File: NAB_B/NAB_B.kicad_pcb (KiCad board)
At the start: 2 copper layers, 35 x 30 mm, 44 parts, among them K1 кнопка, K2 кнопка, X1 Check_point

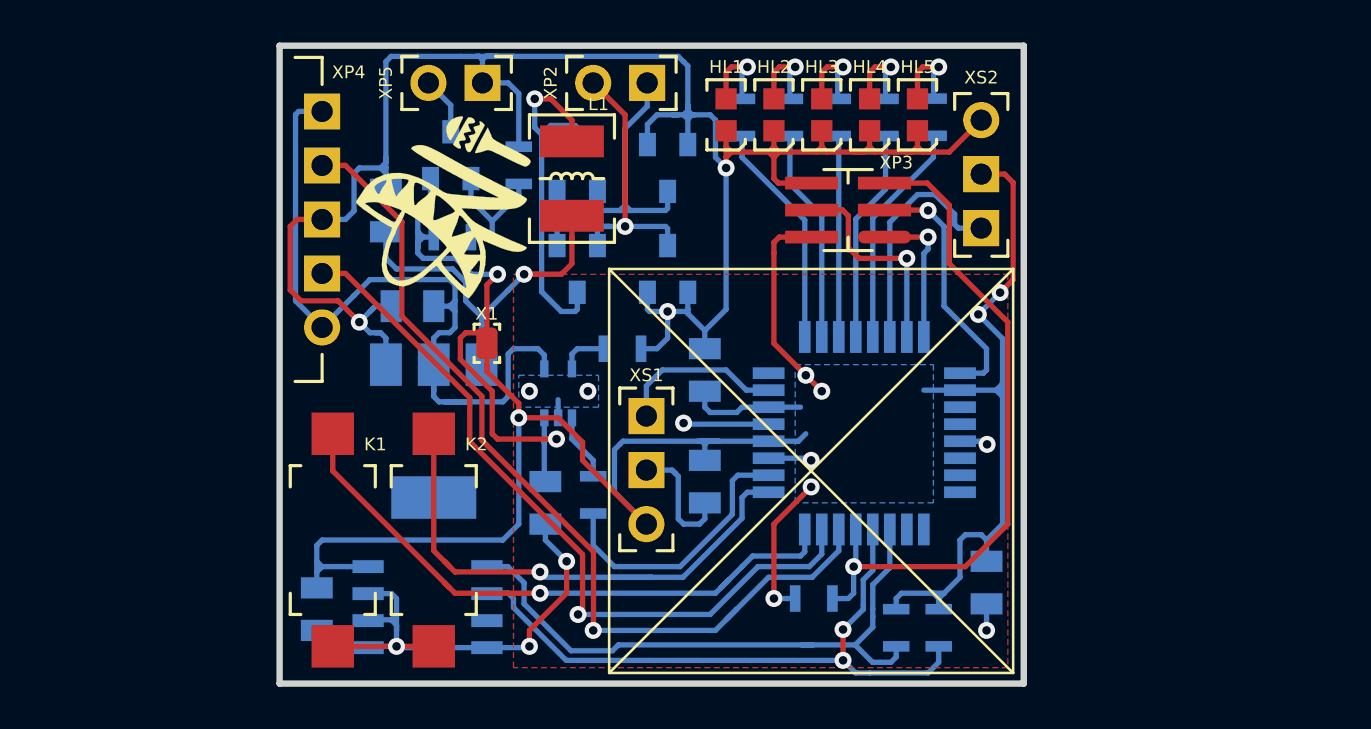
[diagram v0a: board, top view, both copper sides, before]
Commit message: NAB_A: добавить оцифровку заряда, NAB_B: прототип взят от _A
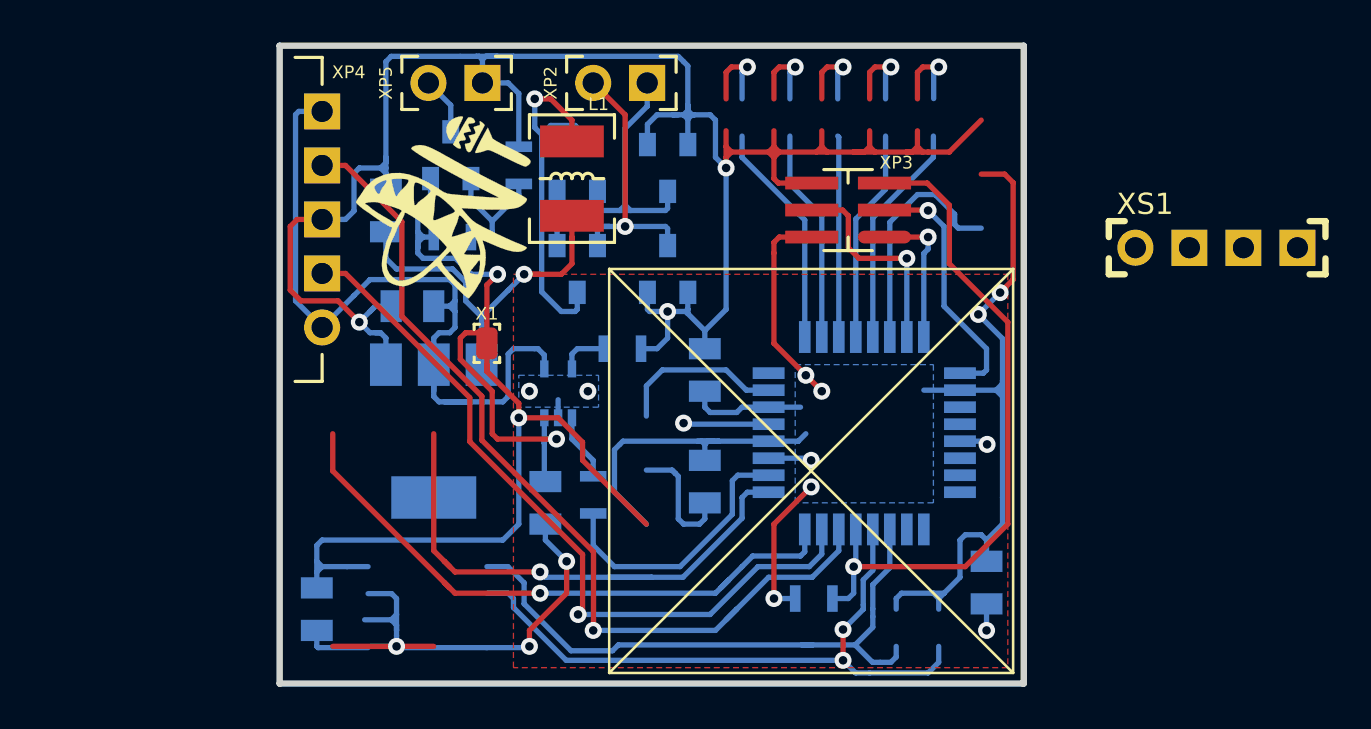
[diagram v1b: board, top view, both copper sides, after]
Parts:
- removed BK1: Преобразователь_температуры_LM75AD, N_DD:SO-8
- removed HL1, HL2, HL3, HL4, HL5: Светодиод, N_VD_HL:Светодиод_SMD_0603
- removed K1, K2: кнопка, N_X:Кнопка_FSMSM
- removed R1, R11, R12, R2, R3, R4, R5: Резистор_0,065Вт, N_RLC:Резистор_SMD_0603_0,065_Вт
- removed XS2: Розетка_PBS3, N_X:Розетка_PBS3_вертикальная
- XS1: value Розетка_PBS3 -> Розетка_PBS4; footprint N_X:Розетка_PBS3_вертикальная -> N_X:Вилка_PLS4_вертикальная
- moved XS1 26.4 mm to (250.2, 49.5), turned to 0 degrees
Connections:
- XS1 pad 1: /MC_VCC -> Net-(XS1-Pad1)
- XS1 pad 2: /GND -> Net-(XS1-Pad2)
- XS1 pad 3: /TX_DATA -> Net-(XS1-Pad3)

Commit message: NAB_B: сформированы требования к плате
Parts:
- removed the XP4 at (212.0, 43.1)
- added K1: кнопка, N_X:Кнопка_FSMSM, F.Cu at (212.5, 58.2)
- added K2: кнопка, N_X:Кнопка_FSMSM, F.Cu at (217.2, 58.2)
- added R3: Резистор_0,065Вт, N_RLC:Резистор_SMD_0603_0,065_Вт, B.Cu at (232.5, 67.5)
- added R4: Резистор_0,065Вт, N_RLC:Резистор_SMD_0603_0,065_Вт, B.Cu at (234.8, 65.8)
- added X2: Check_point, N_X:Пробник, F.Cu at (221.8, 54.0)
- added XP1: Вилка_PLS6, N_X:Вилка_PLS6_вертикальная, F.Cu at (212.0, 42.5)
- moved XS1 50.0 mm to (200.2, 51.5)
- moved R5 7.11 mm to (229.0, 67.2)
- moved C5 1.75 mm to (243.2, 62.5)
- moved L1 1.03 mm to (224.0, 45.5)
- moved DD1 1.00 mm to (233.2, 60.0)
- moved XP4 1.00 mm to (236.5, 49.0)
- moved LOGO1 0.50 mm to (218.2, 47.5)
- renumbered C3 to C1, C1 to C2, C5 to C3, C2 to C4, C6 to C5, C4 to C6, DD2 to G2, R13 to R1, R14 to R2, R9 to R5, R10 to R7, VT2 to VT1, XP5 to XP3, XP3 to XP4
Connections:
- net /TX_DATA renamed Net-(DD1-Pad7)
- DD1 pad 1: /BUT-2 -> /BUTT-2
- DD1 pad 26: Net-(DD1-Pad26) -> /VBAT_MEASUR
- DD1 pad 32: /BUT-1 -> /BUTT-1
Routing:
- net /BUT-1: track 29.6 -> 0.00 mm, vias 1 -> 0
- net /BUTT-1: track 0.00 -> 28.9 mm, vias 0 -> 1
- net /BUT-2: track 26.3 -> 0.00 mm, vias 1 -> 0
- net /BUTT-2: track 0.00 -> 25.8 mm, vias 0 -> 1
- net /MC_VCC: track 103.9 -> 123.8 mm
- net /MC_TX: track 35.6 -> 51.9 mm
- net /VBAT_MEASUR: track 0.00 -> 13.2 mm, vias 0 -> 2
- net Net-(DD1-Pad7): track 7.87 -> 0.00 mm
- net /nRESET: track 32.8 -> 40.3 mm
- net /GND: track 147.6 -> 151.9 mm, vias 12 -> 14
- net /SCL: track 30.7 -> 34.6 mm
- net /5V: track 37.3 -> 38.6 mm
- net /SDA: track 29.1 -> 30.4 mm
- net /V_BAT: track 25.7 -> 26.9 mm
- net /CHARGE_STATUS: track 12.9 -> 13.9 mm
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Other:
- board text added: "5V"
- board text added: "DATA"
- board text added: "R"
- board text added: "RX"
- board text added: "TX"
- board text added: "VCC"
